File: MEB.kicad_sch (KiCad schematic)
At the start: 4 parts

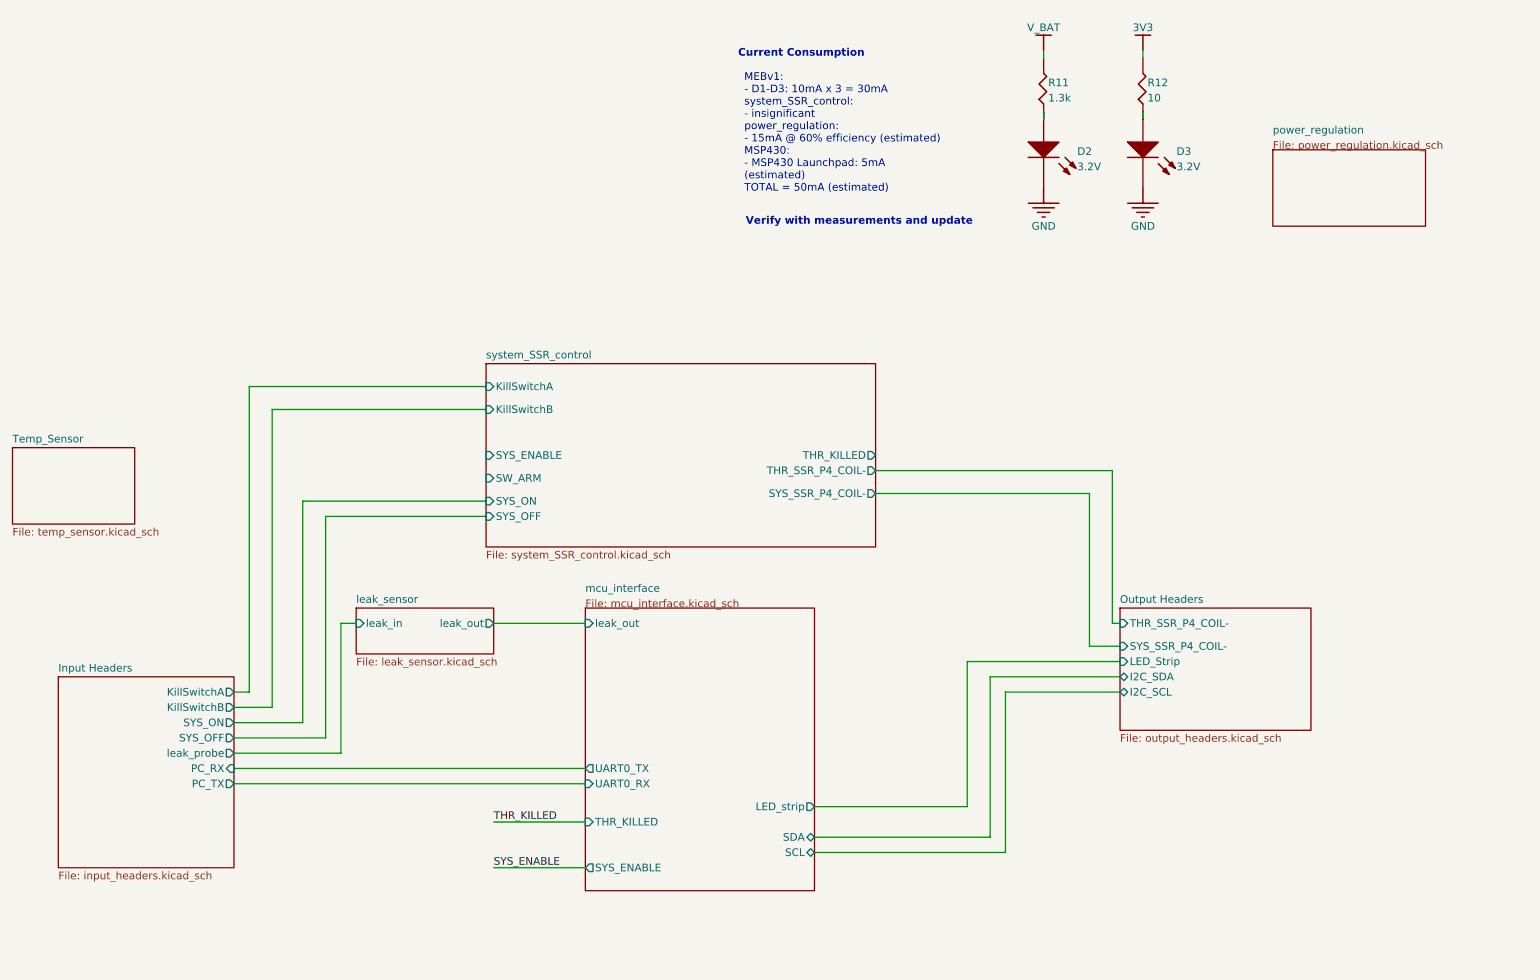
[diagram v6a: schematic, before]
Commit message: updated top level schematic for MEB
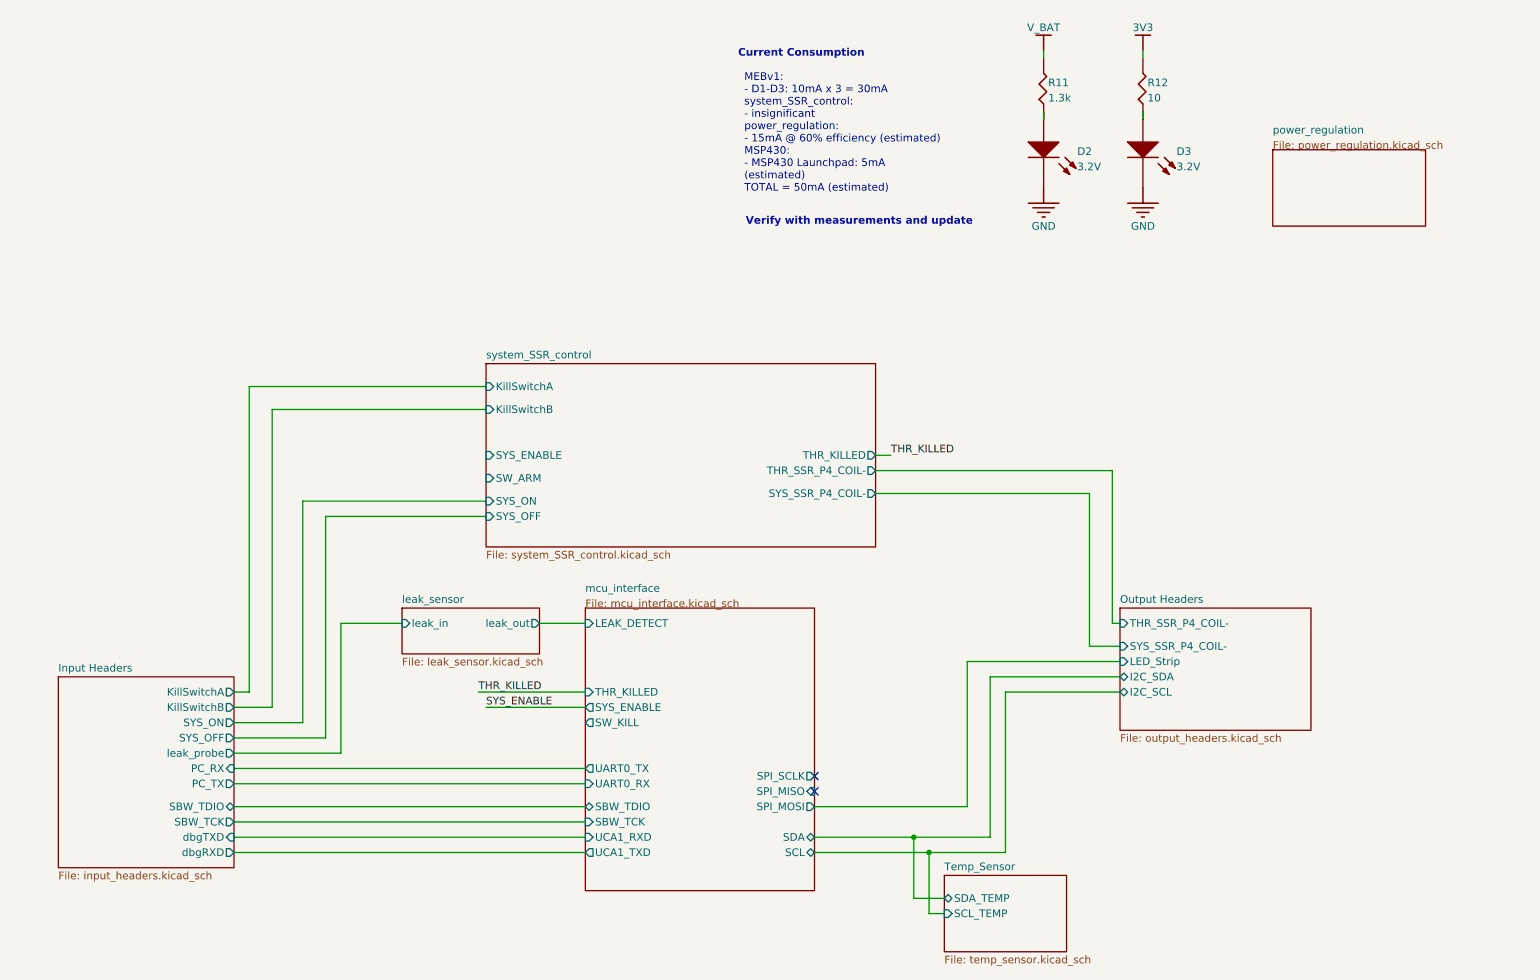
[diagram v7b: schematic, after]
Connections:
- no-connect marks 0 -> 2
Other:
- sheet Input Headers ports: added SBW_TCK, SBW_TDIO, dbgRXD, dbgTXD; removed none
- sheet Temp_Sensor ports: added SCL_TEMP, SDA_TEMP; removed none
- sheet mcu_interface ports: added LEAK_DETECT, SBW_TCK, SBW_TDIO, SPI_MISO, SPI_MOSI, SPI_SCLK, SW_KILL, UCA1_RXD, UCA1_TXD; removed LED_strip, leak_out
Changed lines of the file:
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@@
 (kicad_sch (version 20230121) (generator eeschema)
   (paper "A")
+  (junction (at 168.91 191.77) (diameter 0) (color 0 0 0 0)
+  )
+  (junction (at 171.45 194.31) (diameter 0) (color 0 0 0 0)
+  )
+  (no_connect (at 152.4 184.15))
+  (no_connect (at 152.4 181.61))
   (wire (pts (xy 67.31 135.89) (xy 97.79 135.89))
     (stroke (width 0) (type default))
   )
+  (wire (pts (xy 168.91 191.77) (xy 152.4 191.77))
+    (stroke (width 0) (type default))
+  )
   (wire (pts (xy 55.88 170.18) (xy 62.23 170.18))
+    (stroke (width 0) (type default))
+  )
+  (wire (pts (xy 55.88 194.31) (xy 114.3 194.31))
     (stroke (width 0) (type default))
   )
@@
     (stroke (width 0.254) (type default))
   )
+  (wire (pts (xy 55.88 186.69) (xy 114.3 186.69))
+    (stroke (width 0) (type default))
+  )
   (wire (pts (xy 203.2 162.56) (xy 177.8 162.56))
     (stroke (width 0) (type default))
@@
     (stroke (width 0) (type default))
   )
+  (wire (pts (xy 106.68 156.21) (xy 114.3 156.21))
+    (stroke (width 0) (type default))
+  )
   (wire (pts (xy 203.2 165.1) (xy 181.61 165.1))
     (stroke (width 0) (type default))
@@
   )
   (wire (pts (xy 73.66 177.8) (xy 73.66 156.21))
+    (stroke (width 0) (type default))
+  )
+  (wire (pts (xy 171.45 204.47) (xy 171.45 194.31))
     (stroke (width 0) (type default))
   )
@@
     (stroke (width 0) (type default))
   )
+  (wire (pts (xy 55.88 191.77) (xy 114.3 191.77))
+    (stroke (width 0) (type default))
+  )
   (wire (pts (xy 62.23 170.18) (xy 62.23 120.65))
     (stroke (width 0) (type default))
   )
+  (wire (pts (xy 152.4 186.69) (xy 177.8 186.69))
+    (stroke (width 0) (type default))
+  )
   (wire (pts (xy 203.2 167.64) (xy 184.15 167.64))
     (stroke (width 0) (type default))
   )
-  (wire (pts (xy 184.15 194.31) (xy 152.4 194.31))
+  (wire (pts (xy 184.15 194.31) (xy 171.45 194.31))
+    (stroke (width 0) (type default))
+  )
+  (wire (pts (xy 152.4 194.31) (xy 171.45 194.31))
+    (stroke (width 0) (type default))
+  )
+  (wire (pts (xy 173.99 204.47) (xy 171.45 204.47))
     (stroke (width 0) (type default))
   )
@@
     (stroke (width 0) (type default))
   )
+  (wire (pts (xy 173.99 201.93) (xy 168.91 201.93))
+    (stroke (width 0) (type default))
+  )
   (wire (pts (xy 201.93 130.81) (xy 201.93 156.21))
     (stroke (width 0) (type default))
   )
-  (wire (pts (xy 177.8 186.69) (xy 152.4 186.69))
-    (stroke (width 0) (type default))
-  )
-  (wire (pts (xy 114.3 196.85) (xy 99.06 196.85))
+  (wire (pts (xy 97.79 170.18) (xy 114.3 170.18))
     (stroke (width 0.254) (type default))
+  )
+  (wire (pts (xy 168.91 201.93) (xy 168.91 191.77))
+    (stroke (width 0) (type default))
   )
   (wire (pts (xy 198.12 160.02) (xy 203.2 160.02))
@@
     (stroke (width 0) (type default))
   )
-  (wire (pts (xy 181.61 191.77) (xy 152.4 191.77))
+  (wire (pts (xy 162.56 128.27) (xy 165.1 128.27))
+    (stroke (width 0) (type default))
+  )
+  (wire (pts (xy 181.61 191.77) (xy 168.91 191.77))
     (stroke (width 0) (type default))
   )
@@
   (wire (pts (xy 177.8 162.56) (xy 177.8 186.69))
     (stroke (width 0) (type default))
+  )
+  (wire (pts (xy 96.52 167.64) (xy 114.3 167.64))
+    (stroke (width 0.254) (type default))
   )
   (wire (pts (xy 190.5 60.96) (xy 190.5 62.23))
     (stroke (width 0.254) (type default))
   )
+  (wire (pts (xy 55.88 189.23) (xy 114.3 189.23))
+    (stroke (width 0) (type default))
+  )
   (wire (pts (xy 55.88 167.64) (xy 58.42 167.64))
     (stroke (width 0) (type default))
   )
-  (wire (pts (xy 73.66 156.21) (xy 76.2 156.21))
-    (stroke (width 0) (type default))
-  )
-  (wire (pts (xy 99.06 156.21) (xy 114.3 156.21))
-    (stroke (width 0.254) (type default))
-  )
-  (wire (pts (xy 114.3 189.23) (xy 99.06 189.23))
-    (stroke (width 0.254) (type default))
+  (wire (pts (xy 73.66 156.21) (xy 83.82 156.21))
+    (stroke (width 0) (type default))
   )
   (wire (pts (xy 55.88 175.26) (xy 71.12 175.26))
@@
     (effects (font (size 1.27 1.27) bold) (justify left bottom))
   )
-  (label "SYS_ENABLE" (at 99.06 196.85 0) (fields_autoplaced)
+  (label "THR_KILLED" (at 165.1 128.27 0) (fields_autoplaced)
     (effects (font (size 1.27 1.27)) (justify left bottom))
   )
-  (label "THR_KILLED" (at 99.06 189.23 0) (fields_autoplaced)
+  (label "SYS_ENABLE" (at 97.79 170.18 0) (fields_autoplaced)
+    (effects (font (size 1.27 1.27)) (justify left bottom))
+  )
+  (label "THR_KILLED" (at 96.52 167.64 0) (fields_autoplaced)
     (effects (font (size 1.27 1.27)) (justify left bottom))
   )
@@
     )
   )
-  (sheet (at 76.2 153.67) (size 22.86 7.62) (fields_autoplaced)
+  (sheet (at 83.82 153.67) (size 22.86 7.62) (fields_autoplaced)
     (stroke (width 0) (type solid) (color 128 0 0 1))
     (fill (color 213 166 189 1.0000))
-    (property "Sheetname" "leak_sensor" (at 76.2 152.9584 0)
+    (property "Sheetname" "leak_sensor" (at 83.82 152.9584 0)
       (effects (font (size 1.27 1.27)) (justify left bottom))
     )
-    (property "Sheetfile" "leak_sensor.kicad_sch" (at 76.2 161.8746 0)
+    (property "Sheetfile" "leak_sensor.kicad_sch" (at 83.82 161.8746 0)
       (effects (font (size 1.27 1.27)) (justify left top))
     )
-    (pin "leak_out" output (at 99.06 156.21 0)
+    (pin "leak_out" output (at 106.68 156.21 0)
       (effects (font (size 1.27 1.27)) (justify right))
     )
-    (pin "leak_in" input (at 76.2 156.21 180)
+    (pin "leak_in" input (at 83.82 156.21 180)
       (effects (font (size 1.27 1.27)) (justify left))
     )
@@
       (effects (font (size 1.27 1.27)) (justify left bottom))
     )
-    (pin "leak_out" input (at 114.3 156.21 180)
-      (effects (font (size 1.27 1.27)) (justify left))
-    )
-    (pin "LED_strip" output (at 152.4 186.69 0)
-      (effects (font (size 1.27 1.27)) (justify right))
-    )
     (pin "SCL" bidirectional (at 152.4 194.31 0)
       (effects (font (size 1.27 1.27)) (justify right))
     )
-    (pin "SYS_ENABLE" output (at 114.3 196.85 180)
+    (pin "SYS_ENABLE" output (at 114.3 170.18 180)
       (effects (font (size 1.27 1.27)) (justify left))
     )
@@
       (effects (font (size 1.27 1.27)) (justify right))
     )
-    (pin "THR_KILLED" input (at 114.3 189.23 180)
+    (pin "THR_KILLED" input (at 114.3 167.64 180)
       (effects (font (size 1.27 1.27)) (justify left))
     )
@@
     (pin "UART0_RX" input (at 114.3 182.88 180)
       (effects (font (size 1.27 1.27)) (justify left))
+    )
+    (pin "SW_KILL" output (at 114.3 172.72 180)
+      (effects (font (size 1.27 1.27)) (justify left))
+    )
+    (pin "LEAK_DETECT" input (at 114.3 156.21 180)
+      (effects (font (size 1.27 1.27)) (justify left))
+    )
+    (pin "UCA1_RXD" input (at 114.3 191.77 180)
+      (effects (font (size 1.27 1.27)) (justify left))
+    )
+    (pin "SBW_TDIO" bidirectional (at 114.3 186.69 180)
+      (effects (font (size 1.27 1.27)) (justify left))
+    )
+    (pin "SBW_TCK" input (at 114.3 189.23 180)
+      (effects (font (size 1.27 1.27)) (justify left))
+    )
+    (pin "SPI_MISO" input (at 152.4 184.15 0)
+      (effects (font (size 1.27 1.27)) (justify right))
+    )
+    (pin "SPI_SCLK" output (at 152.4 181.61 0)
+      (effects (font (size 1.27 1.27)) (justify right))
+    )
+    (pin "UCA1_TXD" output (at 114.3 194.31 180)
+      (effects (font (size 1.27 1.27)) (justify left))
+    )
+    (pin "SPI_MOSI" output (at 152.4 186.69 0)
+      (effects (font (size 1.27 1.27)) (justify right))
     )
     (instances
@@
       (effects (font (size 1.27 1.27)) (justify right))
     )
+    (pin "SBW_TCK" output (at 55.88 189.23 0)
+      (effects (font (size 1.27 1.27)) (justify right))
+    )
+    (pin "dbgTXD" input (at 55.88 191.77 0)
+      (effects (font (size 1.27 1.27)) (justify right))
+    )
+    (pin "SBW_TDIO" bidirectional (at 55.88 186.69 0)
+      (effects (font (size 1.27 1.27)) (justify right))
+    )
+    (pin "dbgRXD" output (at 55.88 194.31 0)
+      (effects (font (size 1.27 1.27)) (justify right))
+    )
     (instances
       (project "MEB"
@@
     )
   )
-  (sheet (at 19.05 127) (size 20.32 12.7) (fields_autoplaced)
+  (sheet (at 173.99 198.12) (size 20.32 12.7) (fields_autoplaced)
     (stroke (width 0.1524) (type solid))
     (fill (color 0 0 0 0.0000))
-    (property "Sheetname" "Temp_Sensor" (at 19.05 126.2884 0)
+    (property "Sheetname" "Temp_Sensor" (at 173.99 197.4084 0)
       (effects (font (size 1.27 1.27)) (justify left bottom))
     )
-    (property "Sheetfile" "temp_sensor.kicad_sch" (at 19.05 140.2846 0)
+    (property "Sheetfile" "temp_sensor.kicad_sch" (at 173.99 211.4046 0)
       (effects (font (size 1.27 1.27)) (justify left top))
     )
+    (pin "SDA_TEMP" bidirectional (at 173.99 201.93 180)
+      (effects (font (size 1.27 1.27)) (justify left))
+    )
+    (pin "SCL_TEMP" input (at 173.99 204.47 180)
+      (effects (font (size 1.27 1.27)) (justify left))
+    )
     (instances
